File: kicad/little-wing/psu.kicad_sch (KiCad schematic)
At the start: 14 parts, among them J1 HRO_TYPE-C-31-M-14, J2 Battery, SW1 Battery, U2 ${ALTIUM_VALUE}

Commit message: Fixes and space optimisations
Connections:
- net VOUT renamed VSYS
- no-connect marks 4 -> 5
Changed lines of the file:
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@@
 	(paper "A4")
+	(junction
+		(at 104.14 72.39)
+		(diameter 0)
+		(color 0 0 0 0)
+	)
 	(junction
 		(at 167.64 125.73)
@@
 	)
 	(junction
-		(at 182.88 74.93)
-		(diameter 0)
-		(color 0 0 0 0)
-	)
-	(junction
 		(at 50.8 45.72)
 		(diameter 0)
@@
 	)
 	(junction
+		(at 50.8 43.18)
+		(diameter 0)
+		(color 0 0 0 0)
+	)
+	(junction
+		(at 165.1 85.09)
+		(diameter 0)
+		(color 0 0 0 0)
+	)
+	(junction
+		(at 165.1 82.55)
+		(diameter 0)
+		(color 0 0 0 0)
+	)
+	(junction
+		(at 104.14 95.25)
+		(diameter 0)
+		(color 0 0 0 0)
+	)
+	(junction
+		(at 167.64 123.19)
+		(diameter 0)
+		(color 0 0 0 0)
+	)
+	(junction
 		(at 88.9 72.39)
+		(diameter 0)
+		(color 0 0 0 0)
+	)
+	(junction
+		(at 91.44 95.25)
+		(diameter 0)
+		(color 0 0 0 0)
+	)
+	(junction
+		(at 91.44 125.73)
 		(diameter 0)
 		(color 0 0 0 0)
@@
 	)
 	(junction
-		(at 50.8 43.18)
-		(diameter 0)
-		(color 0 0 0 0)
-	)
-	(junction
-		(at 165.1 85.09)
-		(diameter 0)
-		(color 0 0 0 0)
-	)
-	(junction
-		(at 165.1 82.55)
-		(diameter 0)
-		(color 0 0 0 0)
-	)
-	(junction
-		(at 104.14 95.25)
-		(diameter 0)
-		(color 0 0 0 0)
-	)
-	(junction
-		(at 167.64 123.19)
-		(diameter 0)
-		(color 0 0 0 0)
-	)
-	(junction
-		(at 91.44 95.25)
-		(diameter 0)
-		(color 0 0 0 0)
-	)
-	(junction
-		(at 91.44 125.73)
-		(diameter 0)
-		(color 0 0 0 0)
-	)
-	(junction
 		(at 60.96 34.29)
 		(diameter 0)
@@
 	)
 	(junction
-		(at 104.14 72.39)
+		(at 182.88 74.93)
 		(diameter 0)
 		(color 0 0 0 0)
@@
 		(at 27.94 66.04)
 	)
+	(no_connect
+		(at 165.1 118.11)
+	)
 	(wire
 		(pts
@@
 	(wire
 		(pts
+			(xy 24.13 113.03) (xy 24.13 114.3)
+		)
+		(stroke
+			(width 0)
+			(type default)
+		)
+	)
+	(wire
+		(pts
+			(xy 182.88 74.93) (xy 182.88 77.47)
+		)
+		(stroke
+			(width 0)
+			(type default)
+		)
+	)
+	(wire
+		(pts
+			(xy 91.44 123.19) (xy 91.44 125.73)
+		)
+		(stroke
+			(width 0)
+			(type default)
+		)
+	)
+	(wire
+		(pts
+			(xy 46.99 95.25) (xy 46.99 101.6)
+		)
+		(stroke
+			(width 0)
+			(type default)
+		)
+	)
+	(wire
+		(pts
+			(xy 24.13 114.3) (xy 24.13 116.84)
+		)
+		(stroke
+			(width 0)
+			(type default)
+		)
+	)
+	(wire
+		(pts
+			(xy 104.14 95.25) (xy 104.14 92.71)
+		)
+		(stroke
+			(width 0)
+			(type default)
+		)
+	)
+	(wire
+		(pts
+			(xy 91.44 95.25) (xy 104.14 95.25)
+		)
+		(stroke
+			(width 0)
+			(type default)
+		)
+	)
+	(wire
+		(pts
+			(xy 88.9 72.39) (xy 104.14 72.39)
+		)
+		(stroke
+			(width 0)
+			(type default)
+		)
+	)
+	(wire
+		(pts
 			(xy 88.9 72.39) (xy 88.9 73.66)
 		)
@@
 	(wire
 		(pts
-			(xy 24.13 113.03) (xy 24.13 114.3)
-		)
-		(stroke
-			(width 0)
-			(type default)
-		)
-	)
-	(wire
-		(pts
-			(xy 182.88 74.93) (xy 182.88 77.47)
-		)
-		(stroke
-			(width 0)
-			(type default)
-		)
-	)
-	(wire
-		(pts
-			(xy 91.44 123.19) (xy 91.44 125.73)
-		)
-		(stroke
-			(width 0)
-			(type default)
-		)
-	)
-	(wire
-		(pts
-			(xy 46.99 95.25) (xy 46.99 101.6)
-		)
-		(stroke
-			(width 0)
-			(type default)
-		)
-	)
-	(wire
-		(pts
-			(xy 24.13 114.3) (xy 24.13 116.84)
-		)
-		(stroke
-			(width 0)
-			(type default)
-		)
-	)
-	(wire
-		(pts
-			(xy 104.14 95.25) (xy 104.14 92.71)
-		)
-		(stroke
-			(width 0)
-			(type default)
-		)
-	)
-	(wire
-		(pts
-			(xy 91.44 95.25) (xy 104.14 95.25)
-		)
-		(stroke
-			(width 0)
-			(type default)
-		)
-	)
-	(wire
-		(pts
-			(xy 205.74 99.06) (xy 205.74 74.93)
-		)
-		(stroke
-			(width 0)
-			(type default)
-		)
-	)
-	(wire
-		(pts
 			(xy 60.96 34.29) (xy 60.96 33.02)
 		)
@@
 	(wire
 		(pts
+			(xy 165.1 74.93) (xy 182.88 74.93)
+		)
+		(stroke
+			(width 0)
+			(type default)
+		)
+	)
+	(wire
+		(pts
 			(xy 104.14 72.39) (xy 104.14 74.93)
 		)
@@
 	(wire
 		(pts
-			(xy 165.1 74.93) (xy 182.88 74.93)
-		)
-		(stroke
-			(width 0)
-			(type default)
-		)
-	)
-	(wire
-		(pts
 			(xy 91.44 99.06) (xy 91.44 95.25)
 		)
@@
 	(wire
 		(pts
+			(xy 182.88 74.93) (xy 205.74 74.93)
+		)
+		(stroke
+			(width 0)
+			(type default)
+		)
+	)
+	(wire
+		(pts
 			(xy 165.1 72.39) (xy 165.1 74.93)
 		)
@@
 	(wire
 		(pts
-			(xy 88.9 72.39) (xy 104.14 72.39)
+			(xy 205.74 74.93) (xy 205.74 99.06)
 		)
 		(stroke
@@
 		(pts
 			(xy 46.99 118.11) (xy 46.99 125.73)
-		)
-		(stroke
-			(width 0)
-			(type default)
-		)
-	)
-	(wire
-		(pts
-			(xy 205.74 74.93) (xy 182.88 74.93)
 		)
 		(stroke
@@
 		(on_board yes)
 		(dnp no)
+		(fields_autoplaced yes)
 		(property "Reference" "#PWR018"
 			(at 123.19 33.02 0)
@@
 			)
 		)
-		(property "Value" "VOUT"
+		(property "Value" "VSYS"
 			(at 123.19 29.21 0)
 			(effects
@@
 			)
 		)
-		(property "Value" "VOUT"
+		(property "Value" "VSYS"
 			(at 182.88 71.12 0)
 			(effects

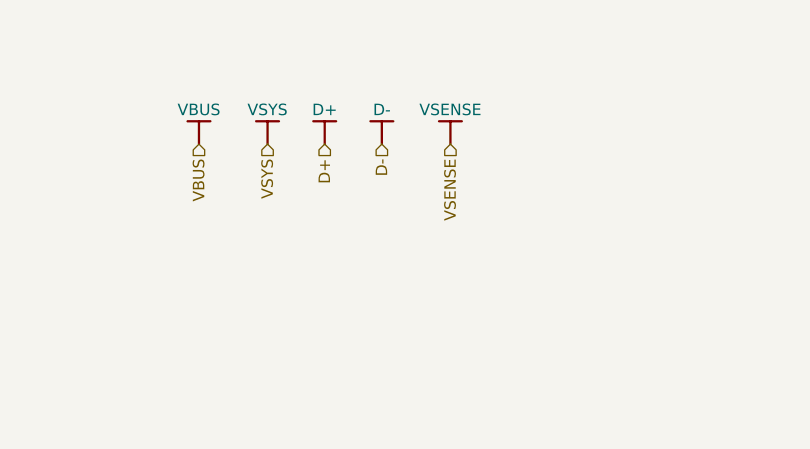
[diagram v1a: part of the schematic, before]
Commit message: Connecting remaining power lines
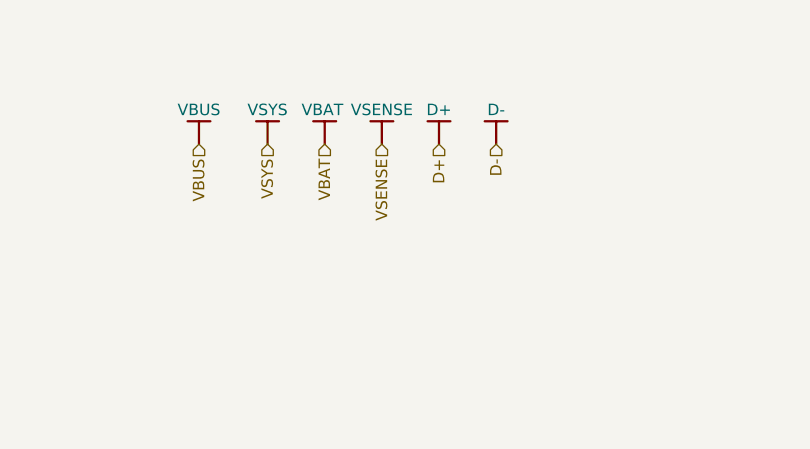
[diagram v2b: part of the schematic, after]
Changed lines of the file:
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@@
 	(hierarchical_label "D+"
 		(shape input)
-		(at 129.54 33.02 270)
+		(at 142.24 33.02 270)
 		(effects
 			(font
@@
 	(hierarchical_label "D-"
 		(shape input)
-		(at 135.89 33.02 270)
+		(at 148.59 33.02 270)
 		(effects
 			(font
@@
 		)
 	)
-	(hierarchical_label "VSENSE"
+	(hierarchical_label "VBAT"
 		(shape input)
-		(at 143.51 33.02 270)
+		(at 129.54 33.02 270)
 		(effects
 			(font
@@
 		)
 	)
+	(hierarchical_label "VSENSE"
+		(shape input)
+		(at 135.89 33.02 270)
+		(effects
+			(font
+				(size 1.27 1.27)
+			)
+			(justify right)
+		)
+	)
 	(symbol
 		(lib_id "npm1100_caax_config1-altium-import:VBUS_BAR")
-		(at 135.89 33.02 180)
+		(at 148.59 33.02 180)
 		(unit 1)
 		(exclude_from_sim no)
@@
 		(dnp no)
 		(property "Reference" "#PWR019"
-			(at 135.89 33.02 0)
+			(at 148.59 33.02 0)
 			(effects
 				(font
@@
 		)
 		(property "Value" "D-"
-			(at 135.89 29.21 0)
+			(at 148.59 29.21 0)
 			(effects
 				(font
@@
 		)
 		(property "Footprint" ""
-			(at 135.89 33.02 0)
+			(at 148.59 33.02 0)
 			(effects
 				(font
@@
 		)
 		(property "Datasheet" ""
-			(at 135.89 33.02 0)
+			(at 148.59 33.02 0)
 			(effects
 				(font
@@
 		)
 		(property "Description" ""
-			(at 135.89 33.02 0)
+			(at 148.59 33.02 0)
 			(effects
 				(font
@@
 	(symbol
 		(lib_id "npm1100_caax_config1-altium-import:VBUS_BAR")
-		(at 129.54 33.02 180)
+		(at 142.24 33.02 180)
 		(unit 1)
 		(exclude_from_sim no)
@@
 		(dnp no)
 		(property "Reference" "#PWR020"
-			(at 129.54 33.02 0)
+			(at 142.24 33.02 0)
 			(effects
 				(font
@@
 		)
 		(property "Value" "D+"
-			(at 129.54 29.21 0)
+			(at 142.24 29.21 0)
 			(effects
 				(font
@@
 		)
 		(property "Footprint" ""
-			(at 129.54 33.02 0)
+			(at 142.24 33.02 0)
 			(effects
 				(font
@@
 		)
 		(property "Datasheet" ""
-			(at 129.54 33.02 0)
+			(at 142.24 33.02 0)
 			(effects
 				(font
@@
 		)
 		(property "Description" ""
-			(at 129.54 33.02 0)
+			(at 142.24 33.02 0)
 			(effects
 				(font
@@
 	(symbol
 		(lib_id "npm1100_caax_config1-altium-import:VOUT_BAR")
-		(at 143.51 33.02 180)
+		(at 135.89 33.02 180)
 		(unit 1)
 		(exclude_from_sim no)
@@
 		(dnp no)
 		(property "Reference" "#PWR063"
-			(at 143.51 33.02 0)
+			(at 135.89 33.02 0)
 			(effects
 				(font
@@
 		)
 		(property "Value" "VSENSE"
-			(at 143.51 29.21 0)
+			(at 135.89 29.21 0)
 			(effects
 				(font
@@
 		)
 		(property "Footprint" ""
-			(at 143.51 33.02 0)
+			(at 135.89 33.02 0)
 			(effects
 				(font
@@
 		)
 		(property "Datasheet" ""
-			(at 143.51 33.02 0)
+			(at 135.89 33.02 0)
 			(effects
 				(font
@@
 		)
 		(property "Description" ""
-			(at 143.51 33.02 0)
+			(at 135.89 33.02 0)
 			(effects
 				(font
@@
 					(unit 1)
 				)
+			)
+		)
+	)
+	(symbol
+		(lib_id "npm1100_caax_config1-altium-import:VOUT_BAR")
+		(at 129.54 33.02 180)
+		(unit 1)
+		(exclude_from_sim no)
+		(in_bom yes)
+		(on_board yes)
+		(dnp no)
+		(property "Reference" "#PWR0132"
+			(at 129.54 33.02 0)
+			(effects
+				(font
+					(size 1.27 1.27)
+				)
+				(hide yes)
+			)
+		)
+		(property "Value" "VBAT"
+			(at 129.286 29.21 0)
+			(effects
+				(font
+					(size 1.27 1.27)
+				)
+			)
+		)
+		(property "Footprint" ""
+			(at 129.54 33.02 0)
+			(effects
+				(font
+					(size 1.27 1.27)
+				)
+			)
+		)
+		(property "Datasheet" ""
+			(at 129.54 33.02 0)
+			(effects
+				(font
+					(size 1.27 1.27)
+				)
+			)
+		)
+		(property "Description" ""
+			(at 129.54 33.02 0)
+			(effects
+				(font
+					(size 1.27 1.27)
+				)
+			)
+		)
+		(pin ""
+		)
+		(instances
+			(project "little-wing"
+				(path "/3a835e6f-a660-4b38-a102-87841cdd95ed/eaaf4618-ba3d-41b4-8a99-4f719e243661/4bfeadaf-0d2e-45fd-a340-a53ab79162c6"
+					(reference "#PWR0132")
+					(unit 1)
+				)

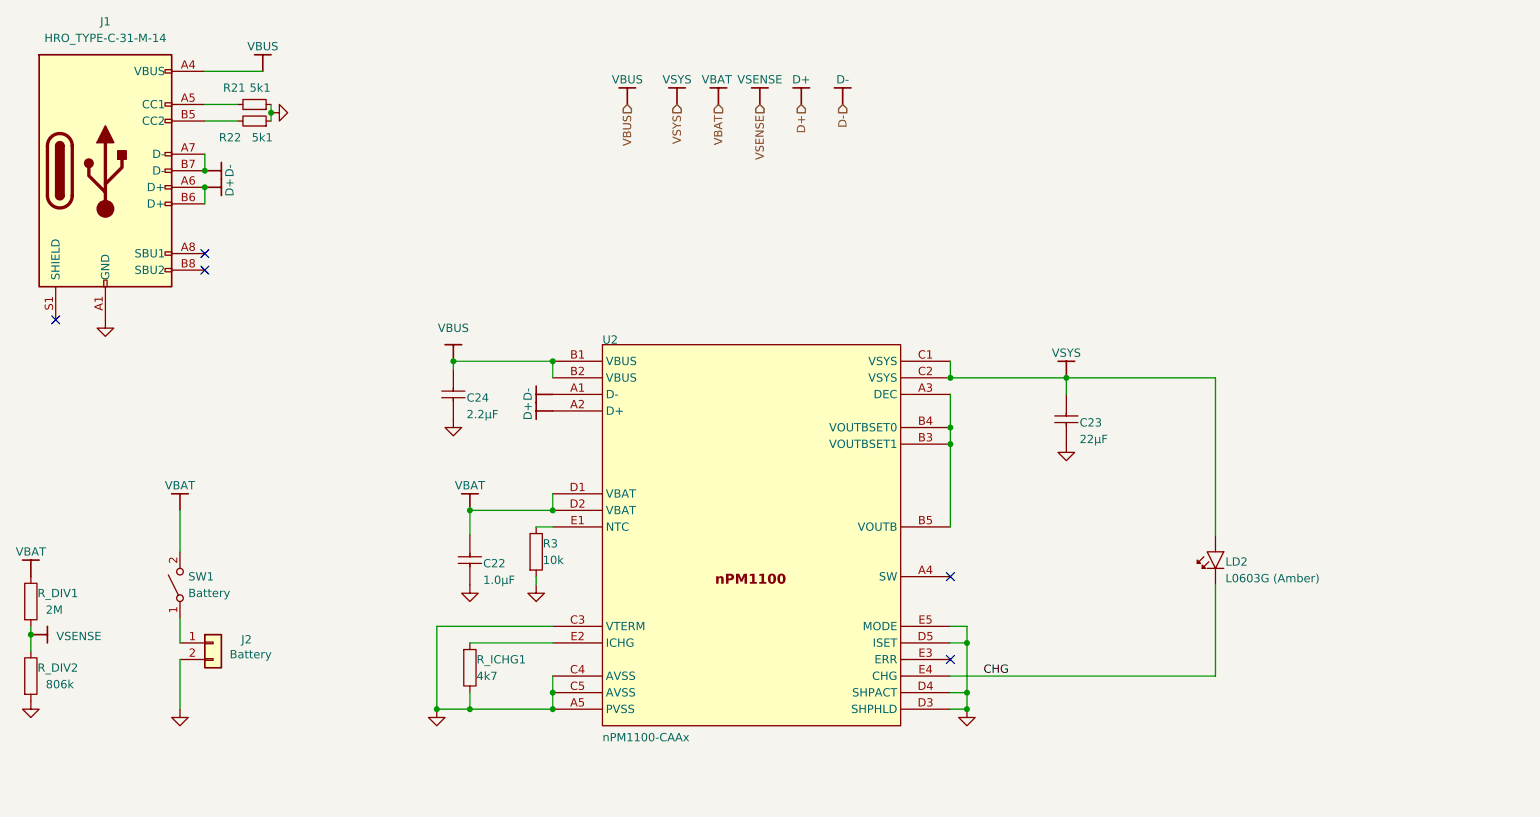
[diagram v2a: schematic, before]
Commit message: Re-organising the schematics sheets a bit
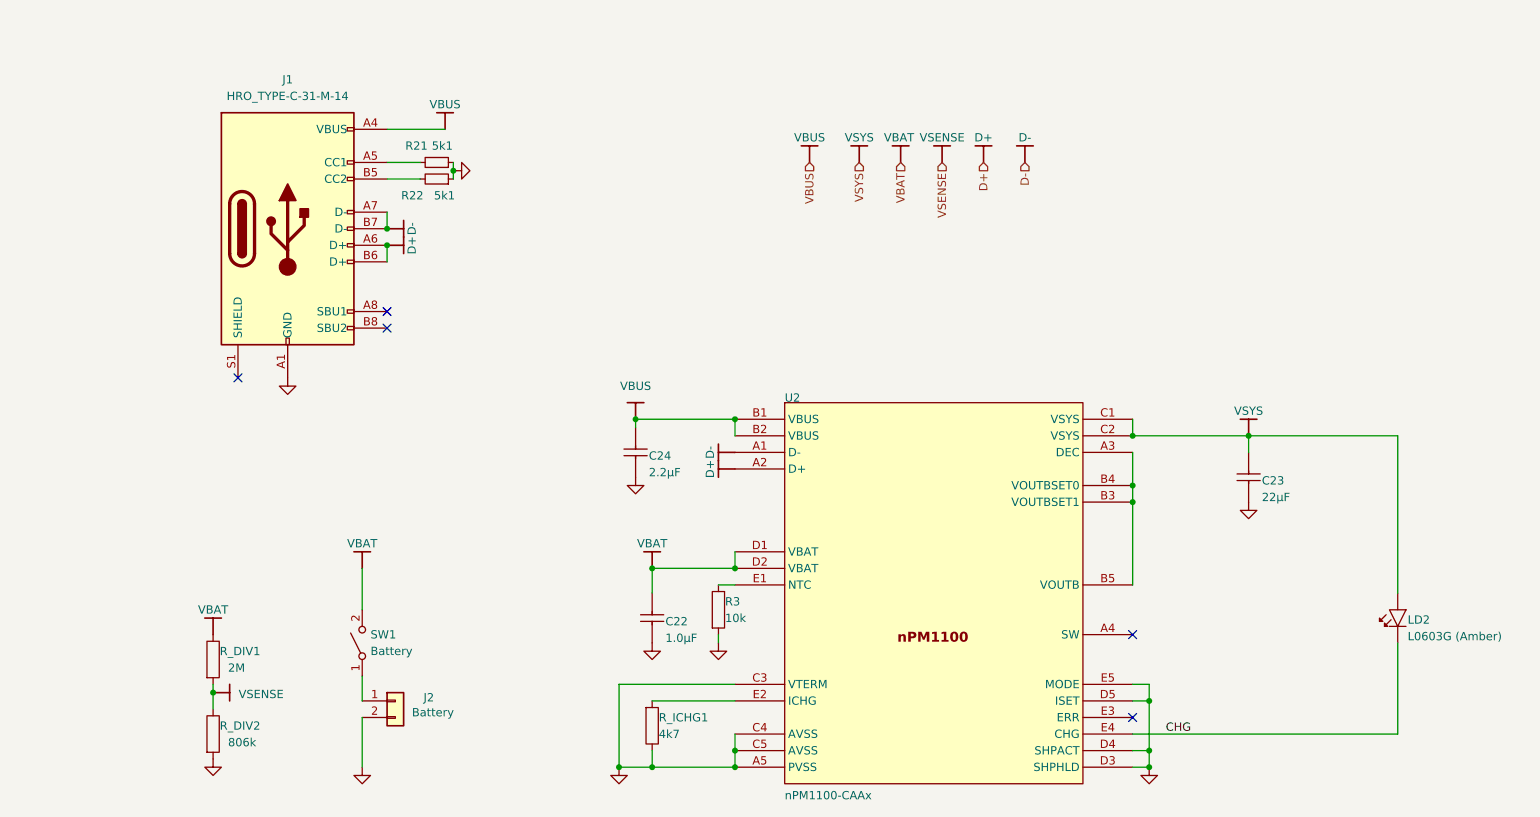
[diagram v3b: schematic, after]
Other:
- moved on the sheet: C22, C23, C24, J1, J2, LD2, R21, R22, R3, R_DIV1, R_DIV2, R_ICHG1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
